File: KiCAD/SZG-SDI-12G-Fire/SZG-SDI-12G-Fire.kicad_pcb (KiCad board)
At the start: 4 copper layers, 70 x 50 mm, 31 parts, among them J1 SYZYGY_TXR-4, J2 Conn_01x06, U1 ATtiny44A-MU

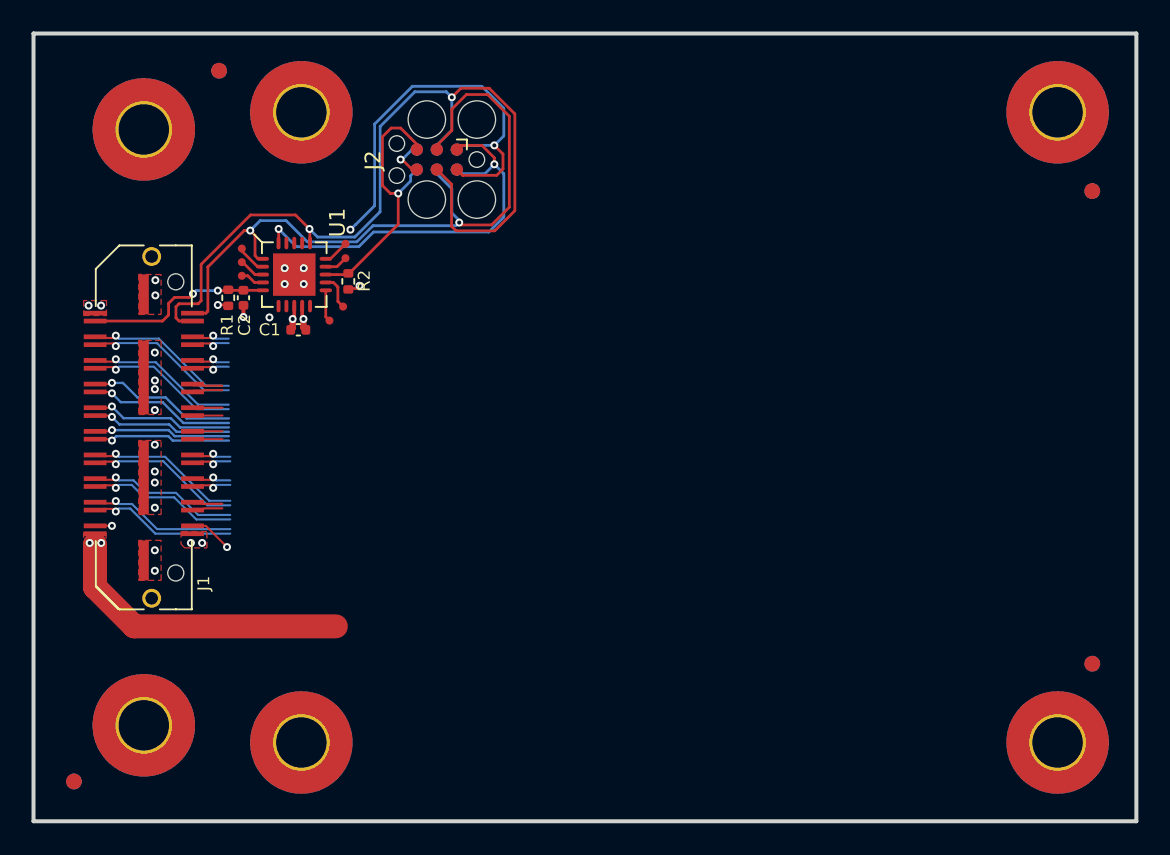
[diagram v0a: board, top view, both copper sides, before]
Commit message: Initial version: Rev.A
Minor schematic tweaks for routing and to address SDI Rx/Tx power rails
PCB fully placed and routed
Added README/CHANGES files
Added CERN-OHL-P v2 license file

Signed-off-by: Charles Steinkuehler <charles@steinkuehler.net>
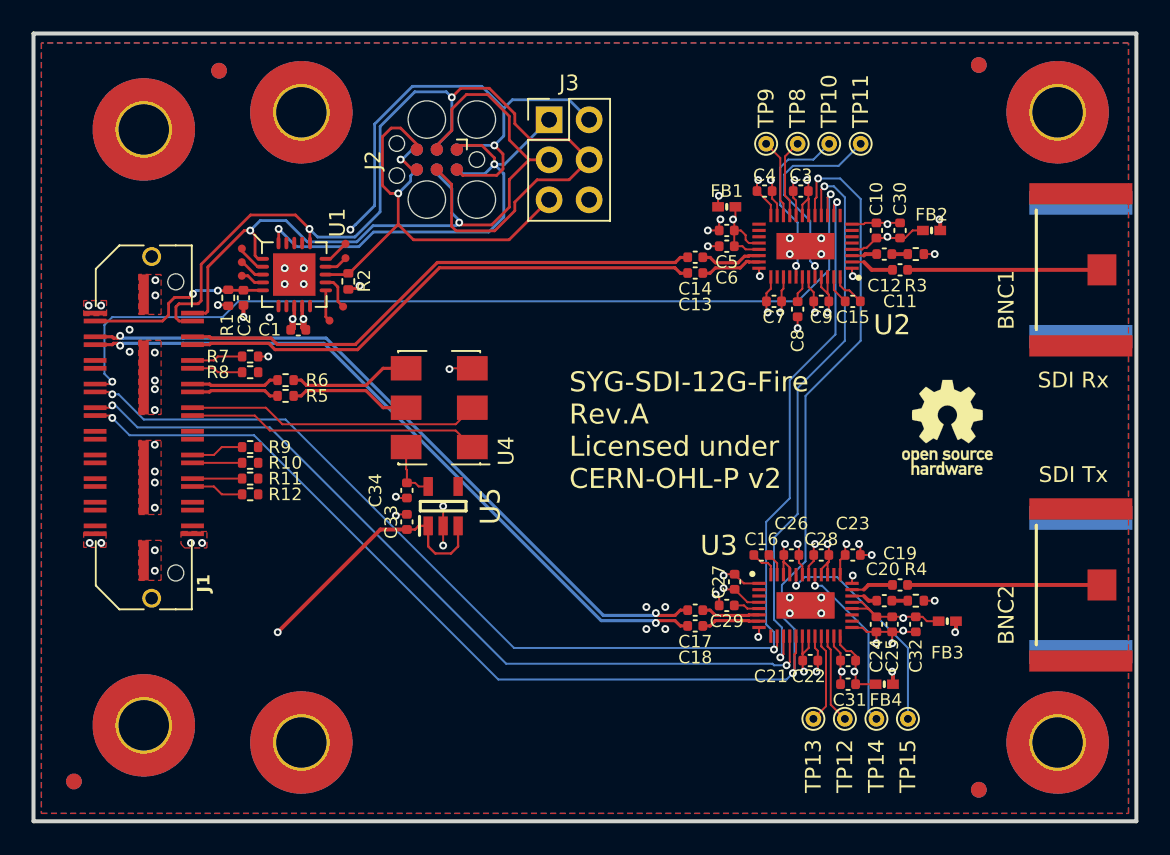
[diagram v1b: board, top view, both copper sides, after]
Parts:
- removed *1: Opal Kelly Logo, okLogo-23x5
- added BNC1: BNC, SYZYGY:BNC7T-J-P-XX-ST-EM1D, F.Cu at (213.5, 96.5)
- added BNC2: BNC, SYZYGY:BNC7T-J-P-XX-ST-EM1D, F.Cu at (213.5, 116.5)
- added C10: 1.0uF, Capacitor_SMD:C_0402_1005Metric, F.Cu at (197.0, 94.0)
- added C11: 4.7uF, Capacitor_SMD:C_0402_1005Metric, F.Cu at (198.5, 96.5)
- added C12: 4.7uF, Capacitor_SMD:C_0402_1005Metric, F.Cu at (197.5, 95.5)
- added C13: 4.7uF, Capacitor_SMD:C_0402_1005Metric, F.Cu at (185.5, 96.7)
- added C14: 4.7uF, Capacitor_SMD:C_0402_1005Metric, F.Cu at (185.5, 95.7)
- added C15: 470nF, Capacitor_SMD:C_0402_1005Metric, F.Cu at (195.5, 98.5)
- added C16: 470nF, Capacitor_SMD:C_0402_1005Metric, F.Cu at (189.7, 114.6)
- added C17: 4.7uF, Capacitor_SMD:C_0402_1005Metric, F.Cu at (185.5, 118.1)
- added C18: 4.7uF, Capacitor_SMD:C_0402_1005Metric, F.Cu at (185.5, 119.1)
- added C19: 4.7uF, Capacitor_SMD:C_0402_1005Metric, F.Cu at (198.5, 116.5)
- added C20: 4.7uF, Capacitor_SMD:C_0402_1005Metric, F.Cu at (197.5, 117.5)
- added C21: 0.1uF, Capacitor_SMD:C_0402_1005Metric, F.Cu at (192.8, 121.3)
- added C22: 0.1uF, Capacitor_SMD:C_0402_1005Metric, F.Cu at (195.2, 121.3)
- added C23: 0.1uF, Capacitor_SMD:C_0402_1005Metric, F.Cu at (195.5, 114.6)
- added C24: 0.1uF, Capacitor_SMD:C_0402_1005Metric, F.Cu at (197.0, 119.0)
- added C25: 0.1uF, Capacitor_SMD:C_0402_1005Metric, F.Cu at (198.0, 119.0)
- added C26: 10uF, Capacitor_SMD:C_0402_1005Metric, F.Cu at (191.6, 114.6)
- added C27: 1.0uF, Capacitor_SMD:C_0402_1005Metric, F.Cu at (188.0, 116.3)
- added C28: 10uF, Capacitor_SMD:C_0402_1005Metric, F.Cu at (193.5, 114.6)
- added C29: 0.1uF, Capacitor_SMD:C_0402_1005Metric, F.Cu at (187.5, 117.8)
- added C3: 0.1uF, Capacitor_SMD:C_0402_1005Metric, F.Cu at (192.2, 91.5)
- added C30: 10uF, Capacitor_SMD:C_0402_1005Metric, F.Cu at (198.5, 94.0)
- added C31: 10uF, Capacitor_SMD:C_0402_1005Metric, F.Cu at (195.2, 122.8)
- added C32: 10uF, Capacitor_SMD:C_0402_1005Metric, F.Cu at (199.5, 119.0)
- added C33: 1.0uF, Capacitor_SMD:C_0402_1005Metric, F.Cu at (167.2, 112.5)
- added C34: 1.0uF, Capacitor_SMD:C_0402_1005Metric, F.Cu at (167.2, 110.5)
- added C4: 0.1uF, Capacitor_SMD:C_0402_1005Metric, F.Cu at (189.9, 91.5)
- added C5: 0.1uF, Capacitor_SMD:C_0402_1005Metric, F.Cu at (187.5, 94.0)
- added C6: 0.1uF, Capacitor_SMD:C_0402_1005Metric, F.Cu at (187.5, 95.0)
- added C7: 0.1uF, Capacitor_SMD:C_0402_1005Metric, F.Cu at (190.5, 98.5)
- added C8: 10uF, Capacitor_SMD:C_0402_1005Metric, F.Cu at (192.0, 99.0)
- added C9: 10uF, Capacitor_SMD:C_0402_1005Metric, F.Cu at (193.5, 98.5)
- added FB1: Ferrite, SYZYGY:BEADC1005X55N, F.Cu at (187.5, 92.5)
- added FB2: Ferrite, SYZYGY:BEADC1005X55N, F.Cu at (200.5, 94.0)
- added FB3: Ferrite, SYZYGY:BEADC1005X55N, F.Cu at (201.5, 118.8)
- added FB4: Ferrite, SYZYGY:BEADC1005X55N, F.Cu at (197.5, 122.8)
- added J3: Conn_02x03_Odd_Even, Connector_PinHeader_2.54mm:PinHeader_2x03_P2.54mm_Vertical, F.Cu at (176.2, 86.9)
- added R10: 0R, Resistor_SMD:R_0402_1005Metric, F.Cu at (157.3, 108.7)
- added R11: 0R, Resistor_SMD:R_0402_1005Metric, F.Cu at (157.3, 109.7)
- added R12: 0R, Resistor_SMD:R_0402_1005Metric, F.Cu at (157.3, 110.7)
- added R3: 2.0R, Resistor_SMD:R_0402_1005Metric, F.Cu at (199.5, 95.5)
- added R4: 75R, Resistor_SMD:R_0402_1005Metric, F.Cu at (199.5, 117.5)
- added R5: 0R, Resistor_SMD:R_0402_1005Metric, F.Cu at (159.5, 104.5)
- added R6: 0R, Resistor_SMD:R_0402_1005Metric, F.Cu at (159.5, 103.5)
- added R7: 0R, Resistor_SMD:R_0402_1005Metric, F.Cu at (157.3, 102.0)
- added R8: 0R, Resistor_SMD:R_0402_1005Metric, F.Cu at (157.3, 103.0)
- added R9: 0R, Resistor_SMD:R_0402_1005Metric, F.Cu at (157.3, 107.7)
- added REF**: OSHW-Logo_5.7x6mm_SilkScreen, Symbol:OSHW-Logo_5.7x6mm_SilkScreen, F.Cu at (201.5, 106.5)
- added TP1: TestPoint, SYZYGY:TestPoint-20mil, F.Cu at (156.7, 96.8)
- added TP12: TestPoint, TestPoint:TestPoint_THTPad_D1.0mm_Drill0.5mm, F.Cu at (195.0, 125.0)
- added TP13: TestPoint, TestPoint:TestPoint_THTPad_D1.0mm_Drill0.5mm, F.Cu at (193.0, 125.0)
- added TP14: TestPoint, TestPoint:TestPoint_THTPad_D1.0mm_Drill0.5mm, F.Cu at (197.0, 125.0)
- added TP15: TestPoint, TestPoint:TestPoint_THTPad_D1.0mm_Drill0.5mm, F.Cu at (199.0, 125.0)
- added TP2: TestPoint, SYZYGY:TestPoint-20mil, F.Cu at (156.7, 96.0)
- added TP3: TestPoint, SYZYGY:TestPoint-20mil, F.Cu at (156.7, 95.1)
- added TP4: TestPoint, SYZYGY:TestPoint-20mil, F.Cu at (163.3, 94.8)
- added U2: GS12241-INE3, SYZYGY:QFN40P600X400X100-41N-D, F.Cu at (192.5, 95.0)
- added U3: GS12281-INTE3, SYZYGY:QFN40P600X400X100-41N-D, F.Cu at (192.5, 117.8)
- added U4: 513FCA000270AAG, SYZYGY:Si513-A, F.Cu at (169.3, 105.2)
- added U5: LP5907MFX-2.5/NOPB, SamacSys:SOT95P280X145-5N, F.Cu at (169.5, 111.5)
- TP10, TP11, TP8, TP9: footprint SYZYGY:TestPoint-20mil -> TestPoint:TestPoint_THTPad_D1.0mm_Drill0.5mm
- moved TP10 37.9 mm to (194.0, 88.5)
- moved TP8 36.1 mm to (192.0, 88.5)
- moved TP11 33.3 mm to (196.0, 88.5)
- moved TP9 27.7 mm to (190.0, 88.5)
- moved FID1 10.8 mm to (203.5, 129.5)
- moved FID2 10.8 mm to (203.5, 83.5)
- moved FID7 10.8 mm to (203.5, 83.5)
- moved FID8 10.8 mm to (203.5, 129.5)
- moved TP6 6.72 mm to (163.2, 98.8)
- moved TP7 3.08 mm to (163.3, 95.7)
- renumbered REF** to LOGO1, G*** to LOGO2
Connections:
- net /MCU_MISO renamed /AVR/MCU_MISO
- net /MCU_RESET_B renamed /AVR/MCU_RESET_B
- H1 pad 1: unconnected-(H1-Pad1) -> GND
- H2 pad 1: unconnected-(H2-Pad1) -> GND
- H3 pad 1: unconnected-(H3-Pad1) -> GND
- H4 pad 1: unconnected-(H4-Pad1) -> GND
- H5 pad 1: unconnected-(H5-Pad1) -> GND
- H6 pad 1: unconnected-(H6-Pad1) -> GND
- J1 pad 14: /S0 -> /SDIN
- J1 pad 16: /S1 -> /CS_n
- J1 pad 17: /S2 -> /CLK_FS
- J1 pad 18: /S3 -> /SDOUT
- J1 pad 19: /S4 -> /CLK_OE
- J1 pad 20: /S5 -> /SCLK
- TP10 pad 1: Net-(TP10-Pad1) -> /SDI/GPIO2
- TP11 pad 1: Net-(TP11-Pad1) -> /SDI/GPIO3
- TP6 pad 1: Net-(TP6-Pad1) -> Net-(U1-XTAL2/PB1)
- TP7 pad 1: Net-(TP7-Pad1) -> Net-(U1-PB2)
- TP8 pad 1: Net-(TP8-Pad1) -> /SDI/GPIO1
- TP9 pad 1: Net-(TP9-Pad1) -> /SDI/GPIO0
- U1 pad 12: Net-(TP7-Pad1) -> Net-(U1-XTAL2/PB1)
- U1 pad 14: Net-(TP9-Pad1) -> Net-(U1-PB2)
- U1 pad 15: Net-(TP11-Pad1) -> Net-(U1-PA7)
- U1 pad 2: Net-(TP10-Pad1) -> Net-(U1-PA3)
- U1 pad 3: Net-(TP8-Pad1) -> Net-(U1-PA2)
- U1 pad 4: Net-(TP6-Pad1) -> Net-(U1-PA1)
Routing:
- net /VIO: track 11.1 -> 103.5 mm, vias 2 -> 7
- net /SCLK: track 0.00 -> 92.0 mm, vias 0 -> 3
- net /CS_n: track 0.00 -> 82.2 mm, vias 0 -> 3
- net +3V3: track 69.7 -> 137.1 mm, vias 7 -> 9
- net /SDIN: track 0.00 -> 58.6 mm, vias 0 -> 2
- net /SDOUT: track 0.00 -> 52.7 mm, vias 0 -> 2
- net GND: track 4.35 -> 55.0 mm, vias 20 -> 66
- net /SDI/SDIX: track 0.00 -> 36.2 mm, vias 0 -> 2
- net /TX0P: track 9.33 -> 45.3 mm, vias 1 -> 2
- net /TX0N: track 9.34 -> 45.3 mm, vias 1 -> 2
- net /RX0N: track 1.92 -> 33.9 mm, vias 1 -> 0
- net /RX0P: track 1.91 -> 33.9 mm, vias 1 -> 0
- net +5V: track 26.0 -> 0.00 mm
- net /CLK_FS: track 0.00 -> 18.6 mm
- net /CLK_OE: track 0.00 -> 18.6 mm
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- added copper zone on In2.Cu, net /SDI/VCC_I
- added copper zone on In2.Cu, net /SDI/VCC_O
- added copper zone on B.Cu, net GND
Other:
- board text added: "SDI Rx"
- board text added: "SDI Tx"
- board text added: "SYG-SDI-12G-Fire Rev.A Licensed under CERN-OHL-P v2"
- board text added: "SZG-SDI-12G-Fire Rev.A"
- board text removed: "SZG-TEMPLATE-TXR Rev A"

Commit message: Update with part numbers
Add manufacturer part numbers as ordered from DigiKey
Add stitching vias on PCB for SDI 75 ohm striplines

Signed-off-by: Charles Steinkuehler <charles@steinkuehler.net>
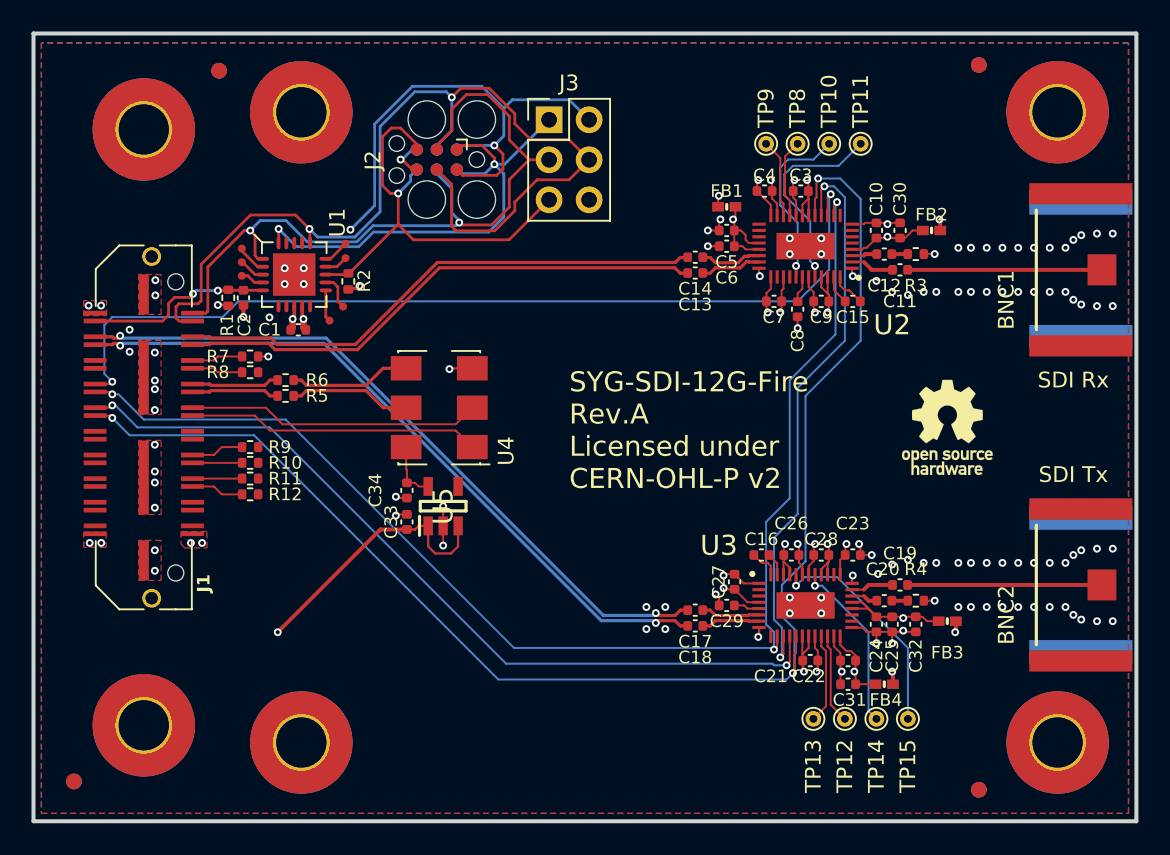
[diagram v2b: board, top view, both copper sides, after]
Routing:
- net GND: vias 66 -> 124
